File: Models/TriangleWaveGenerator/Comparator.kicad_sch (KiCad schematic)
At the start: 3 parts, among them U2 LM311N/NOPB

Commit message: Filled in breadboard schematic, now need purchase links
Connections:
- net Input renamed Input(+)
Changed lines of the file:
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@@
 		)
 	)
-	(hierarchical_label "Input"
+	(hierarchical_label "Input(+)"
 		(shape input)
 		(at 137.16 81.28 180)

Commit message: Did the BOM
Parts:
- C3, C4: footprint (none) -> TwoTerminal:THT_2.54mm; Cost (none) -> $0.82; Cost (qty10) (none) -> $0.479; Purchase Link (none) -> https://www.digikey.com/en/products/detail/murata-electroni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; RoHS Compliant (none) -> YES
- U2: footprint (none) -> IC:PDIP-8; Cost (none) -> $0.92; Cost (qty10) (none) -> $0.663; Purchase Link (none) -> https://www.digikey.com/en/products/detail/texas-instrument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; RoHS Compliant (none) -> YES
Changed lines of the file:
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@@
 			)
 		)
-		(property "Footprint" ""
+		(property "Footprint" "TwoTerminal:THT_2.54mm"
 			(at 171.1452 96.52 0)
 			(effects
@@
 		)
 		(property "Description" "Unpolarized capacitor"
+			(at 170.18 92.71 0)
+			(effects
+				(font
+					(size 1.27 1.27)
+				)
+				(hide yes)
+			)
+		)
+		(property "Purchase Link" "https://www.digikey.com/en/products/detail/murata-electronics/RDE5C1H104J2P1H03B/10706775"
+			(at 170.18 92.71 0)
+			(effects
+				(font
+					(size 1.27 1.27)
+				)
+				(hide yes)
+			)
+		)
+		(property "Cost" "$0.82"
+			(at 170.18 92.71 0)
+			(effects
+				(font
+					(size 1.27 1.27)
+				)
+				(hide yes)
+			)
+		)
+		(property "Cost (qty10)" "$0.479"
+			(at 170.18 92.71 0)
+			(effects
+				(font
+					(size 1.27 1.27)
+				)
+				(hide yes)
+			)
+		)
+		(property "RoHS Compliant" "YES"
 			(at 170.18 92.71 0)
 			(effects
@@
 			)
 		)
-		(property "Footprint" ""
+		(property "Footprint" "IC:PDIP-8"
 			(at 152.4 82.55 0)
 			(effects
@@
 		)
 		(property "Description" ""
+			(at 152.4 82.55 0)
+			(effects
+				(font
+					(size 1.27 1.27)
+				)
+				(hide yes)
+			)
+		)
+		(property "Purchase Link" "https://www.digikey.com/en/products/detail/texas-instruments/LM311N-NOPB/6175"
+			(at 152.4 82.55 0)
+			(effects
+				(font
+					(size 1.27 1.27)
+				)
+				(hide yes)
+			)
+		)
+		(property "Cost" "$0.92"
+			(at 152.4 82.55 0)
+			(effects
+				(font
+					(size 1.27 1.27)
+				)
+				(hide yes)
+			)
+		)
+		(property "Cost (qty10)" "$0.663"
+			(at 152.4 82.55 0)
+			(effects
+				(font
+					(size 1.27 1.27)
+				)
+				(hide yes)
+			)
+		)
+		(property "RoHS Compliant" "YES"
 			(at 152.4 82.55 0)
 			(effects
@@
 			)
 		)
-		(property "Footprint" ""
+		(property "Footprint" "TwoTerminal:THT_2.54mm"
 			(at 130.5052 96.52 0)
 			(effects
@@
 			(at 129.54 92.71 0)
 			(effects
+				(font
+					(size 1.27 1.27)
+				)
+				(hide yes)
+			)
+		)
+		(property "Purchase Link" "https://www.digikey.com/en/products/detail/murata-electronics/RDE5C1H104J2P1H03B/10706775"
+			(at 129.54 92.71 0)
+			(effects
+				(font
+					(size 1.27 1.27)
+				)
+				(hide yes)
+			)
+		)
+		(property "Cost" "$0.82"
+			(at 129.54 92.71 0)
+			(effects
+				(font
+					(size 1.27 1.27)
+				)
+				(hide yes)
+			)
+		)
+		(property "Cost (qty10)" "$0.479"
+			(at 129.54 92.71 0)
+			(effects
+				(font
+					(size 1.27 1.27)
+				)
+				(hide yes)
+			)
+		)
+		(property "RoHS Compliant" "YES"
+			(at 129.54 92.71 0)
+			(effects

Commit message: Fix the schematic
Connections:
- net 15V: now also C3.2; no longer C3.1
- net GND: now also C3.1; no longer C3.2
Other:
- moved on the sheet: C3
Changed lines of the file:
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@@
 	(paper "A4")
 	(junction
-		(at 170.18 86.36)
+		(at 170.18 78.74)
 		(diameter 0)
 		(color 0 0 0 0)
@@
 	(wire
 		(pts
+			(xy 170.18 76.2) (xy 170.18 78.74)
+		)
+		(stroke
+			(width 0)
+			(type default)
+		)
+	)
+	(wire
+		(pts
 			(xy 129.54 86.36) (xy 129.54 88.9)
 		)
@@
 	(wire
 		(pts
-			(xy 170.18 78.74) (xy 170.18 81.28)
+			(xy 167.64 78.74) (xy 170.18 78.74)
+		)
+		(stroke
+			(width 0)
+			(type default)
+		)
+	)
+	(wire
+		(pts
+			(xy 170.18 78.74) (xy 172.72 78.74)
+		)
+		(stroke
+			(width 0)
+			(type default)
+		)
+	)
+	(wire
+		(pts
+			(xy 170.18 83.82) (xy 170.18 86.36)
 		)
 		(stroke
@@
 	(wire
 		(pts
-			(xy 170.18 86.36) (xy 170.18 88.9)
-		)
-		(stroke
-			(width 0)
-			(type default)
-		)
-	)
-	(wire
-		(pts
 			(xy 129.54 86.36) (xy 137.16 86.36)
 		)
@@
 	(wire
 		(pts
-			(xy 170.18 86.36) (xy 172.72 86.36)
-		)
-		(stroke
-			(width 0)
-			(type default)
-		)
-	)
-	(wire
-		(pts
-			(xy 170.18 96.52) (xy 170.18 99.06)
-		)
-		(stroke
-			(width 0)
-			(type default)
-		)
-	)
-	(wire
-		(pts
-			(xy 167.64 78.74) (xy 170.18 78.74)
+			(xy 167.64 83.82) (xy 170.18 83.82)
+		)
+		(stroke
+			(width 0)
+			(type default)
+		)
+	)
+	(wire
+		(pts
+			(xy 170.18 66.04) (xy 170.18 68.58)
+		)
+		(stroke
+			(width 0)
+			(type default)
+		)
+	)
+	(wire
+		(pts
+			(xy 127 86.36) (xy 129.54 86.36)
 		)
 		(stroke
@@
 		(pts
 			(xy 167.64 86.36) (xy 170.18 86.36)
-		)
-		(stroke
-			(width 0)
-			(type default)
-		)
-	)
-	(wire
-		(pts
-			(xy 167.64 81.28) (xy 170.18 81.28)
-		)
-		(stroke
-			(width 0)
-			(type default)
-		)
-	)
-	(wire
-		(pts
-			(xy 127 86.36) (xy 129.54 86.36)
 		)
 		(stroke
@@
 	(hierarchical_label "Output"
 		(shape output)
-		(at 167.64 83.82 0)
+		(at 167.64 81.28 0)
 		(effects
 			(font
@@
 	(hierarchical_label "15V"
 		(shape input)
-		(at 172.72 86.36 0)
+		(at 172.72 78.74 0)
 		(effects
 			(font
@@
 	(symbol
 		(lib_id "Device:C")
-		(at 170.18 92.71 0)
+		(at 170.18 72.39 0)
 		(unit 1)
 		(exclude_from_sim no)
@@
 		(fields_autoplaced yes)
 		(property "Reference" "C3"
-			(at 173.99 91.4399 0)
+			(at 173.99 71.1199 0)
 			(effects
 				(font
@@
 		)
 		(property "Value" "100 nF"
-			(at 173.99 93.9799 0)
+			(at 173.99 73.6599 0)
 			(effects
 				(font
@@
 		)
 		(property "Footprint" "TwoTerminal:THT_2.54mm"
-			(at 171.1452 96.52 0)
+			(at 171.1452 76.2 0)
 			(effects
 				(font
@@
 		)
 		(property "Datasheet" "~"
-			(at 170.18 92.71 0)
+			(at 170.18 72.39 0)
 			(effects
 				(font
@@
 		)
 		(property "Description" "Unpolarized capacitor"
-			(at 170.18 92.71 0)
+			(at 170.18 72.39 0)
 			(effects
 				(font
@@
 		)
 		(property "Purchase Link" "https://www.digikey.com/en/products/detail/murata-electronics/RDE5C1H104J2P1H03B/10706775"
-			(at 170.18 92.71 0)
+			(at 170.18 72.39 0)
 			(effects
 				(font
@@
 		)
 		(property "Cost" "$0.82"
-			(at 170.18 92.71 0)
+			(at 170.18 72.39 0)
 			(effects
 				(font
@@
 		)
 		(property "Cost (qty10)" "$0.479"
-			(at 170.18 92.71 0)
+			(at 170.18 72.39 0)
 			(effects
 				(font
@@
 		)
 		(property "RoHS Compliant" "YES"
-			(at 170.18 92.71 0)
+			(at 170.18 72.39 0)
 			(effects
 				(font
@@
 	(symbol
 		(lib_id "power:GND")
-		(at 170.18 99.06 0)
+		(at 170.18 66.04 180)
 		(unit 1)
 		(exclude_from_sim no)
@@
 		(fields_autoplaced yes)
 		(property "Reference" "#PWR04"
-			(at 170.18 105.41 0)
+			(at 170.18 59.69 0)
 			(effects
 				(font
@@
 		)
 		(property "Value" "GND"
-			(at 170.18 104.14 0)
-			(effects
-				(font
-					(size 1.27 1.27)
-				)
+			(at 172.72 64.7699 0)
+			(effects
+				(font
+					(size 1.27 1.27)
+				)
+				(justify right)
 			)
 		)
 		(property "Footprint" ""
-			(at 170.18 99.06 0)
+			(at 170.18 66.04 0)
 			(effects
 				(font
@@
 		)
 		(property "Datasheet" ""
-			(at 170.18 99.06 0)
+			(at 170.18 66.04 0)
 			(effects
 				(font
@@
 		)
 		(property "Description" "Power symbol creates a global label with name \"GND\" , ground"
-			(at 170.18 99.06 0)
-			(effects
-				(font
+			(at 170.18 66.04 0)
+			(effects
+				(font

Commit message: Return to this later
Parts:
- added R5: 4.7k, symbol Device:R_US
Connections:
- net -15V: now also U2.1 (GND)
- net 15V: now also R5.2
- net GND: no longer U2.1 (GND)
- net Output: now also R5.1
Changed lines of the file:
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@@
 	(paper "A4")
+	(junction
+		(at 175.26 81.28)
+		(diameter 0)
+		(color 0 0 0 0)
+	)
 	(junction
 		(at 170.18 78.74)
@@
 	(wire
 		(pts
+			(xy 175.26 81.28) (xy 177.8 81.28)
+		)
+		(stroke
+			(width 0)
+			(type default)
+		)
+	)
+	(wire
+		(pts
 			(xy 170.18 83.82) (xy 170.18 86.36)
 		)
@@
 	(wire
 		(pts
+			(xy 175.26 91.44) (xy 175.26 93.98)
+		)
+		(stroke
+			(width 0)
+			(type default)
+		)
+	)
+	(wire
+		(pts
 			(xy 167.64 83.82) (xy 170.18 83.82)
 		)
@@
 	(wire
 		(pts
+			(xy 175.26 81.28) (xy 175.26 83.82)
+		)
+		(stroke
+			(width 0)
+			(type default)
+		)
+	)
+	(wire
+		(pts
+			(xy 167.64 81.28) (xy 175.26 81.28)
+		)
+		(stroke
+			(width 0)
+			(type default)
+		)
+	)
+	(wire
+		(pts
 			(xy 127 86.36) (xy 129.54 86.36)
 		)
@@
 			(width 0)
 			(type default)
-		)
-	)
-	(hierarchical_label "Output"
-		(shape output)
-		(at 167.64 81.28 0)
-		(effects
-			(font
-				(size 1.27 1.27)
-			)
-			(justify left)
 		)
 	)
@@
 	(hierarchical_label "-15V"
 		(shape input)
+		(at 137.16 78.74 180)
+		(effects
+			(font
+				(size 1.27 1.27)
+			)
+			(justify right)
+		)
+	)
+	(hierarchical_label "Output"
+		(shape output)
+		(at 177.8 81.28 0)
+		(effects
+			(font
+				(size 1.27 1.27)
+			)
+			(justify left)
+		)
+	)
+	(hierarchical_label "-15V"
+		(shape input)
 		(at 127 86.36 180)
+		(effects
+			(font
+				(size 1.27 1.27)
+			)
+			(justify right)
+		)
+	)
+	(hierarchical_label "15V"
+		(shape input)
+		(at 175.26 93.98 270)
 		(effects
 			(font
@@
 	)
 	(symbol
+		(lib_id "Device:R_US")
+		(at 175.26 87.63 0)
+		(unit 1)
+		(exclude_from_sim no)
+		(in_bom yes)
+		(on_board yes)
+		(dnp no)
+		(fields_autoplaced yes)
+		(property "Reference" "R5"
+			(at 177.8 86.3599 0)
+			(effects
+				(font
+					(size 1.27 1.27)
+				)
+				(justify left)
+			)
+		)
+		(property "Value" "4.7k"
+			(at 177.8 88.8999 0)
+			(effects
+				(font
+					(size 1.27 1.27)
+				)
+				(justify left)
+			)
+		)
+		(property "Footprint" ""
+			(at 176.276 87.884 90)
+			(effects
+				(font
+					(size 1.27 1.27)
+				)
+				(hide yes)
+			)
+		)
+		(property "Datasheet" "~"
+			(at 175.26 87.63 0)
+			(effects
+				(font
+					(size 1.27 1.27)
+				)
+				(hide yes)
+			)
+		)
+		(property "Description" "Resistor, US symbol"
+			(at 175.26 87.63 0)
+			(effects
+				(font
+					(size 1.27 1.27)
+				)
+				(hide yes)
+			)
+		)
+		(pin "1"
+		)
+		(pin "2"
+		)
+		(instances
+			(project ""
+				(path "/dfa365f3-bdb0-4155-b97b-9be2aee452a3/0809bfcf-3fce-4388-8d70-4aadde866c67"
+					(reference "R5")
+					(unit 1)
+				)
+			)
+		)
+	)
+	(symbol
 		(lib_id "power:GND")
 		(at 137.16 83.82 270)
@@
 					(unit 1)
 				)
-			)
-		)
-	)
-	(symbol
-		(lib_id "power:GND")
-		(at 137.16 78.74 270)
-		(unit 1)
-		(exclude_from_sim no)
-		(in_bom yes)
-		(on_board yes)
-		(dnp no)
-		(fields_autoplaced yes)
-		(property "Reference" "#PWR06"
-			(at 130.81 78.74 0)
-			(effects
-				(font
-					(size 1.27 1.27)
-				)
-				(hide yes)
-			)
-		)
-		(property "Value" "GND"
-			(at 133.35 78.7399 90)
-			(effects
-				(font
-					(size 1.27 1.27)
-				)
-				(justify right)
-			)
-		)
-		(property "Footprint" ""
-			(at 137.16 78.74 0)
-			(effects
-				(font
-					(size 1.27 1.27)
-				)
-				(hide yes)
-			)
-		)
-		(property "Datasheet" ""
-			(at 137.16 78.74 0)
-			(effects
-				(font
-					(size 1.27 1.27)
-				)
-				(hide yes)
-			)
-		)
-		(property "Description" "Power symbol creates a global label with name \"GND\" , ground"
-			(at 137.16 78.74 0)
-			(effects
-				(font
-					(size 1.27 1.27)
-				)
-				(hide yes)
-			)
-		)
-		(pin "1"
-		)
-		(instances
-			(project "TriangleWaveGenerator"
-				(path "/dfa365f3-bdb0-4155-b97b-9be2aee452a3/0809bfcf-3fce-4388-8d70-4aadde866c67"
-					(reference "#PWR06")
-					(unit 1)
-				)

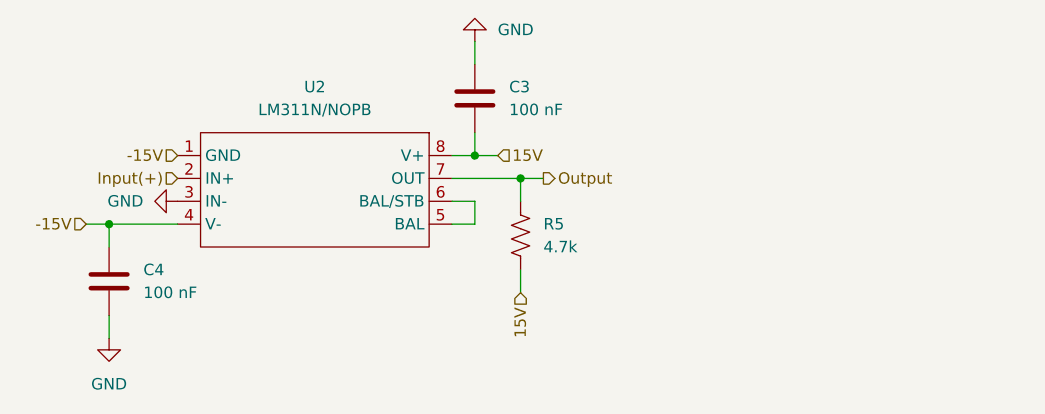
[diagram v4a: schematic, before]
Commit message: Added voltage divider to schematic
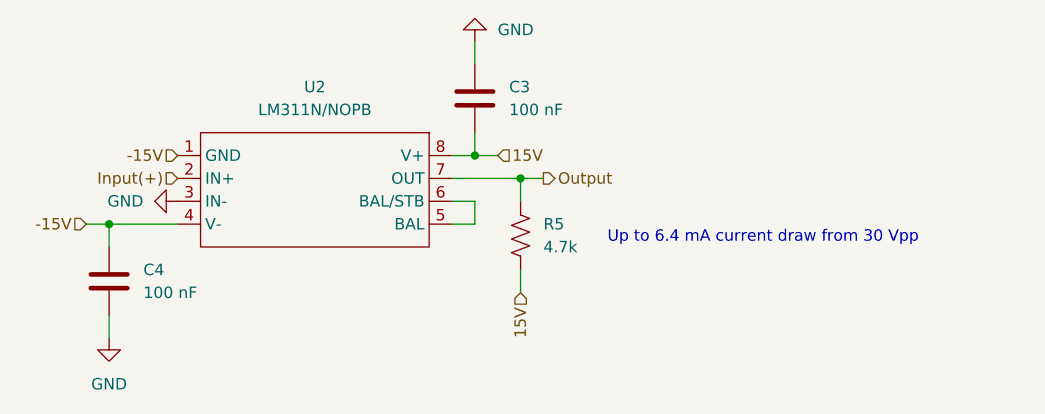
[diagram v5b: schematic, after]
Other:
- note added: "Up to 6.4 mA current draw from 30 Vpp"
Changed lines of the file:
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@@
 	(generator_version "9.0")
 	(paper "A4")
+	(text "Up to 6.4 mA current draw from 30 Vpp"
+		(exclude_from_sim no)
+		(at 184.912 87.122 0)
+		(effects
+			(font
+				(size 1.27 1.27)
+			)
+			(justify left top)
+		)
+	)
 	(junction
 		(at 175.26 81.28)

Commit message: Exclude this from the BOM
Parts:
- R5: now left out of the parts list
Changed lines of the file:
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@@
 		(unit 1)
 		(exclude_from_sim no)
-		(in_bom yes)
+		(in_bom no)
 		(on_board yes)
 		(dnp no)
@@
 			(at 175.26 87.63 0)
 			(effects
+				(font
+					(size 1.27 1.27)
+				)
+				(hide yes)
+			)
+		)
+		(property "Purchase Link" ""
+			(at 175.26 87.63 0)
+			(effects
